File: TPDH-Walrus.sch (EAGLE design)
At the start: 34 parts, among them Q2 DMG3404, U1 MS5803-14BA, U2 SN65HVD33RHL

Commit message: PTH ISP, more routing
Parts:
- ISP1: value AVRISP -> AVRISP-6; device bschulz:AVRISP -> bschulz:AVRISP-6
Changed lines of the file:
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@@
 <part name="GND2" library="SparkFun-PowerSymbols" library_urn="urn:adsk.eagle:library:530" deviceset="GND" device=""/>
 <part name="H2" library="bschulz" deviceset="MOUNTING_HOLE" device="2_NP"/>
-<part name="ISP1" library="bschulz" deviceset="AVRISP" device=""/>
+<part name="ISP1" library="bschulz" deviceset="AVRISP" device="-6" value="AVRISP-6"/>
 <part name="PAD1" library="wirepad" library_urn="urn:adsk.eagle:library:412" deviceset="1,6/0,8" device="" package3d_urn="urn:adsk.eagle:package:30830/1"/>
 <part name="PAD2" library="wirepad" library_urn="urn:adsk.eagle:library:412" deviceset="1,6/0,8" device="" package3d_urn="urn:adsk.eagle:package:30830/1"/>

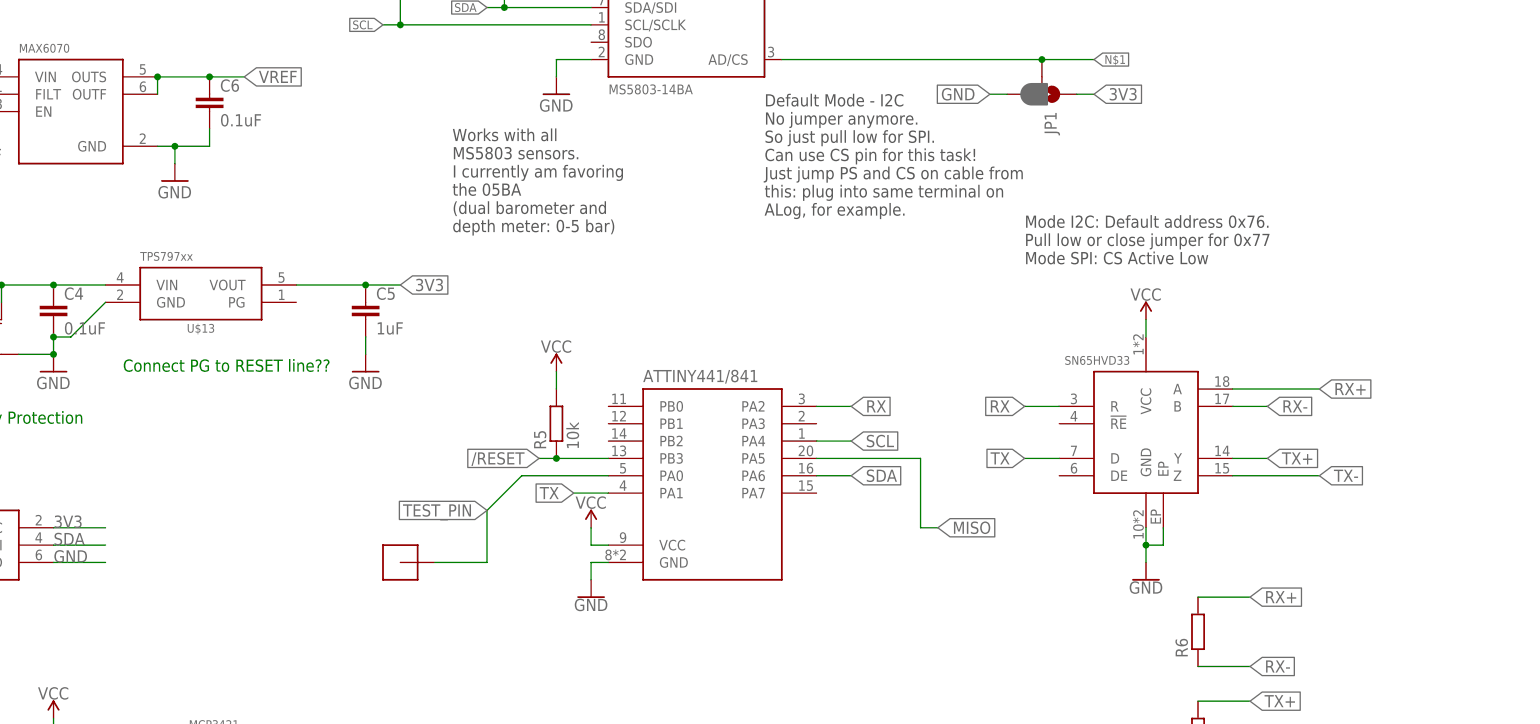
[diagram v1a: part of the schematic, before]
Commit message: multiple schematic and layout updates * status indicator * LDO reset * move thermistor by power supply and voltage reference * rip up traces and reorganize
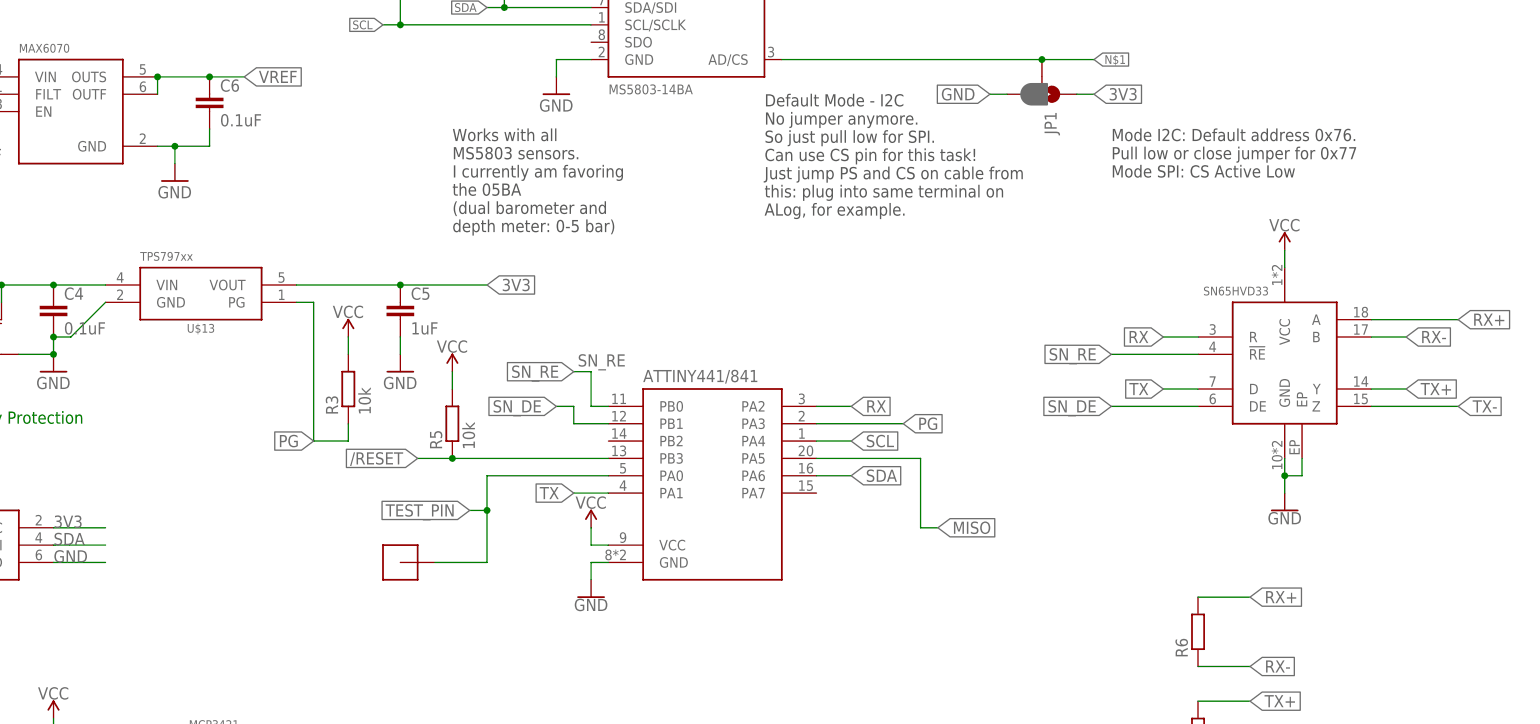
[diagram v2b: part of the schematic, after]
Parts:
- added R3: 10k, bschulz_passives:R-EU_10KR0402
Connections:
- new net PG: R3.1, U$13.PG, U$4.PA3
- new net SN_DE: U$4.PB1, U2.DE
- new net SN_RE: U$4.PB0, U2.!RE
- new net VCC: R3.2
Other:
- note removed: "Connect PG to RESET line??"
- moved on the sheet: C5, R5

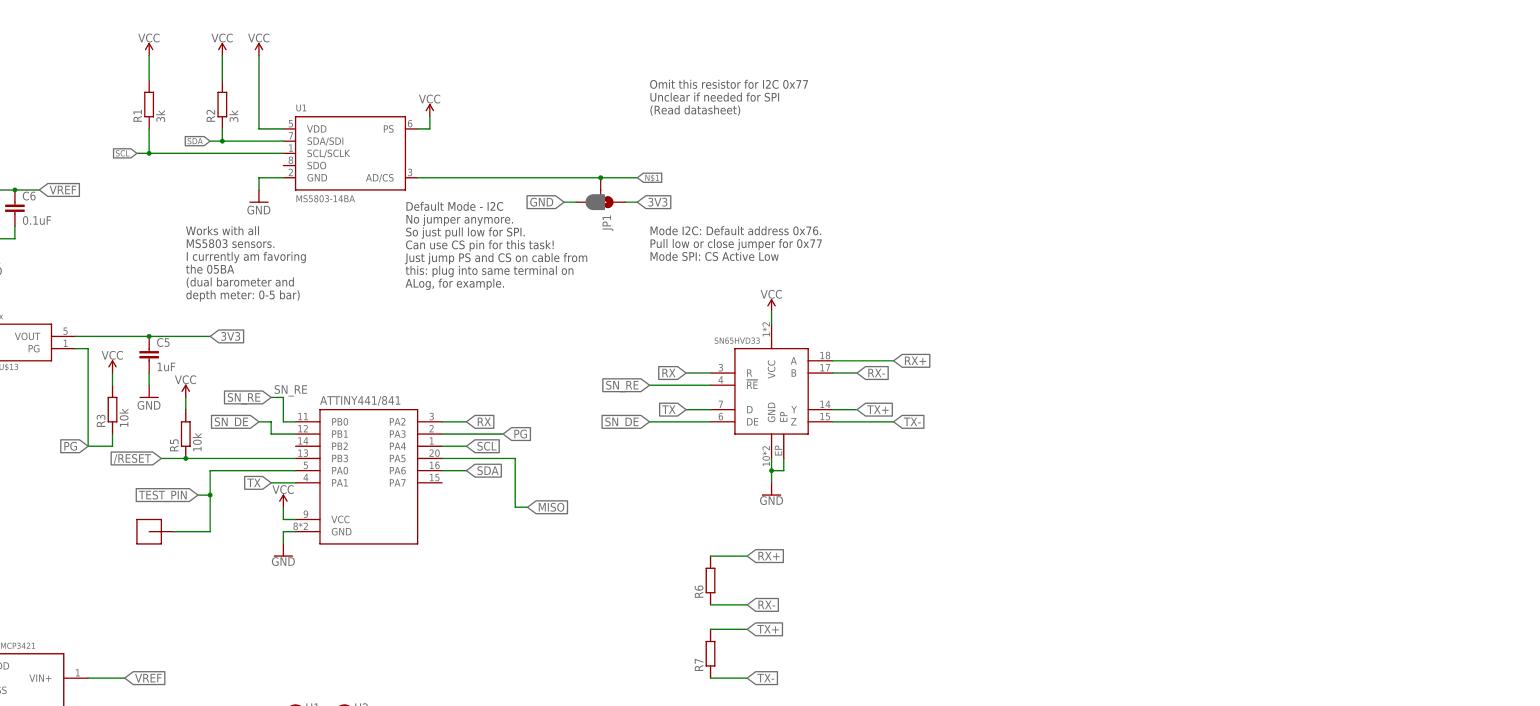
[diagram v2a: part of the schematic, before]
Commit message: ATTiny1634 on schematic
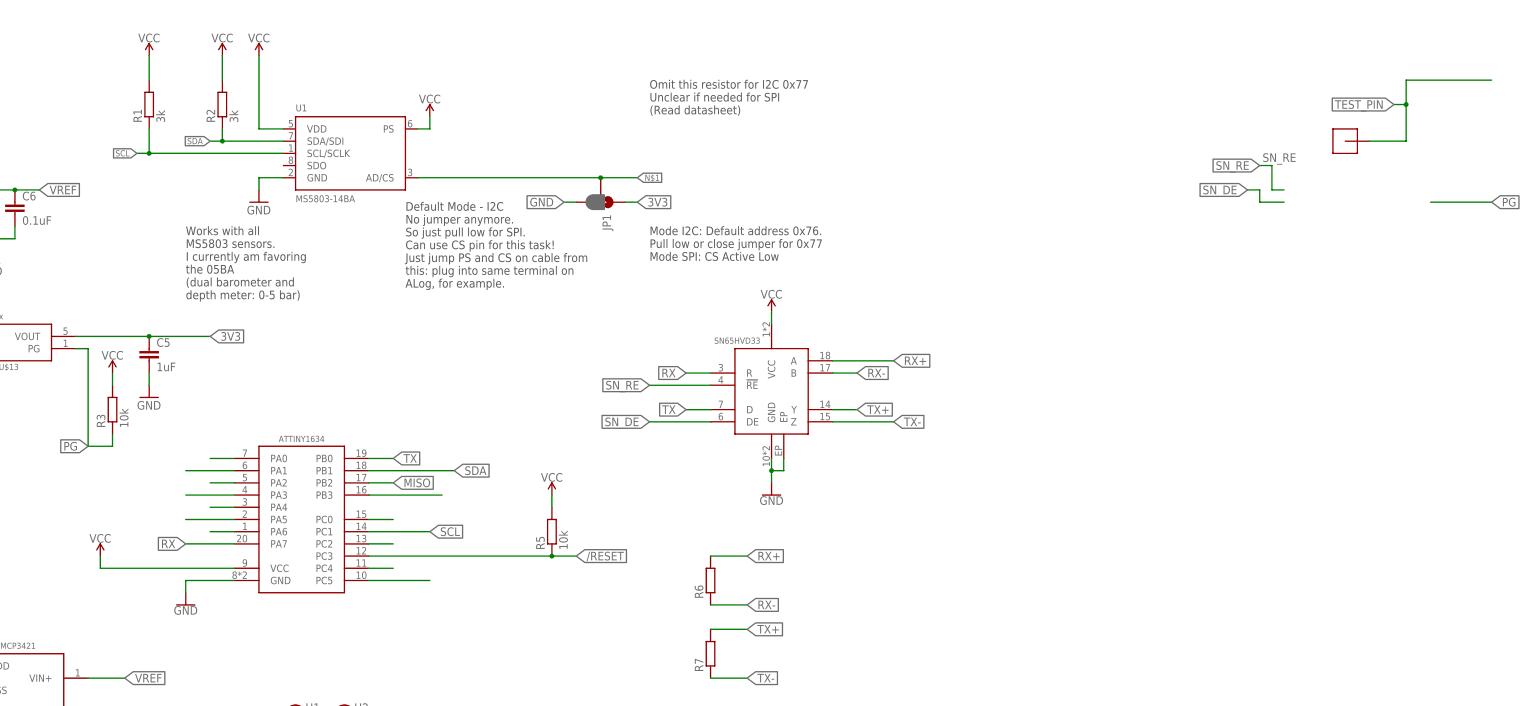
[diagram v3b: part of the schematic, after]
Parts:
- removed U$4: ATTINY441/841VQFN, bschulz:ATTINY441/841VQFN
- added U3: (no value), bschulz:ATTINY1634QFN
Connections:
- new net N$10: U3.PC4
- new net N$12: U3.PC5
- new net N$13: U3.PA4
- new net N$14: U3.PA5
- new net N$15: U3.PA6
- new net N$2: U3.PA0
- new net N$3: U3.PA1
- new net N$5: U3.PB3
- new net N$6: U3.PC0
- new net N$7: U3.PA2
- new net N$8: U3.PC2
- new net N$9: U3.PA3
- net /RESET: now also U3.PC3; no longer U$4.PB3
- net 3V3: now also U3.VCC; no longer U$4.VCC
- net GND: now also U3.GND; no longer U$4.GND
- net MISO: now also U3.PB2; no longer U$4.PA5
- net PG: no longer U$4.PA3
- net RX: now also U3.PA7; no longer U$4.PA2
- net SCL: now also U3.PC1; no longer U$4.PA4
- net SDA: now also U3.PB1; no longer U$4.PA6
- net SN_DE: no longer U$4.PB1
- net SN_RE: no longer U$4.PB0
- net TEST_PIN: no longer U$4.PA0
- net TX: now also U3.PB0; no longer U$4.PA1
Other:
- moved on the sheet: R5

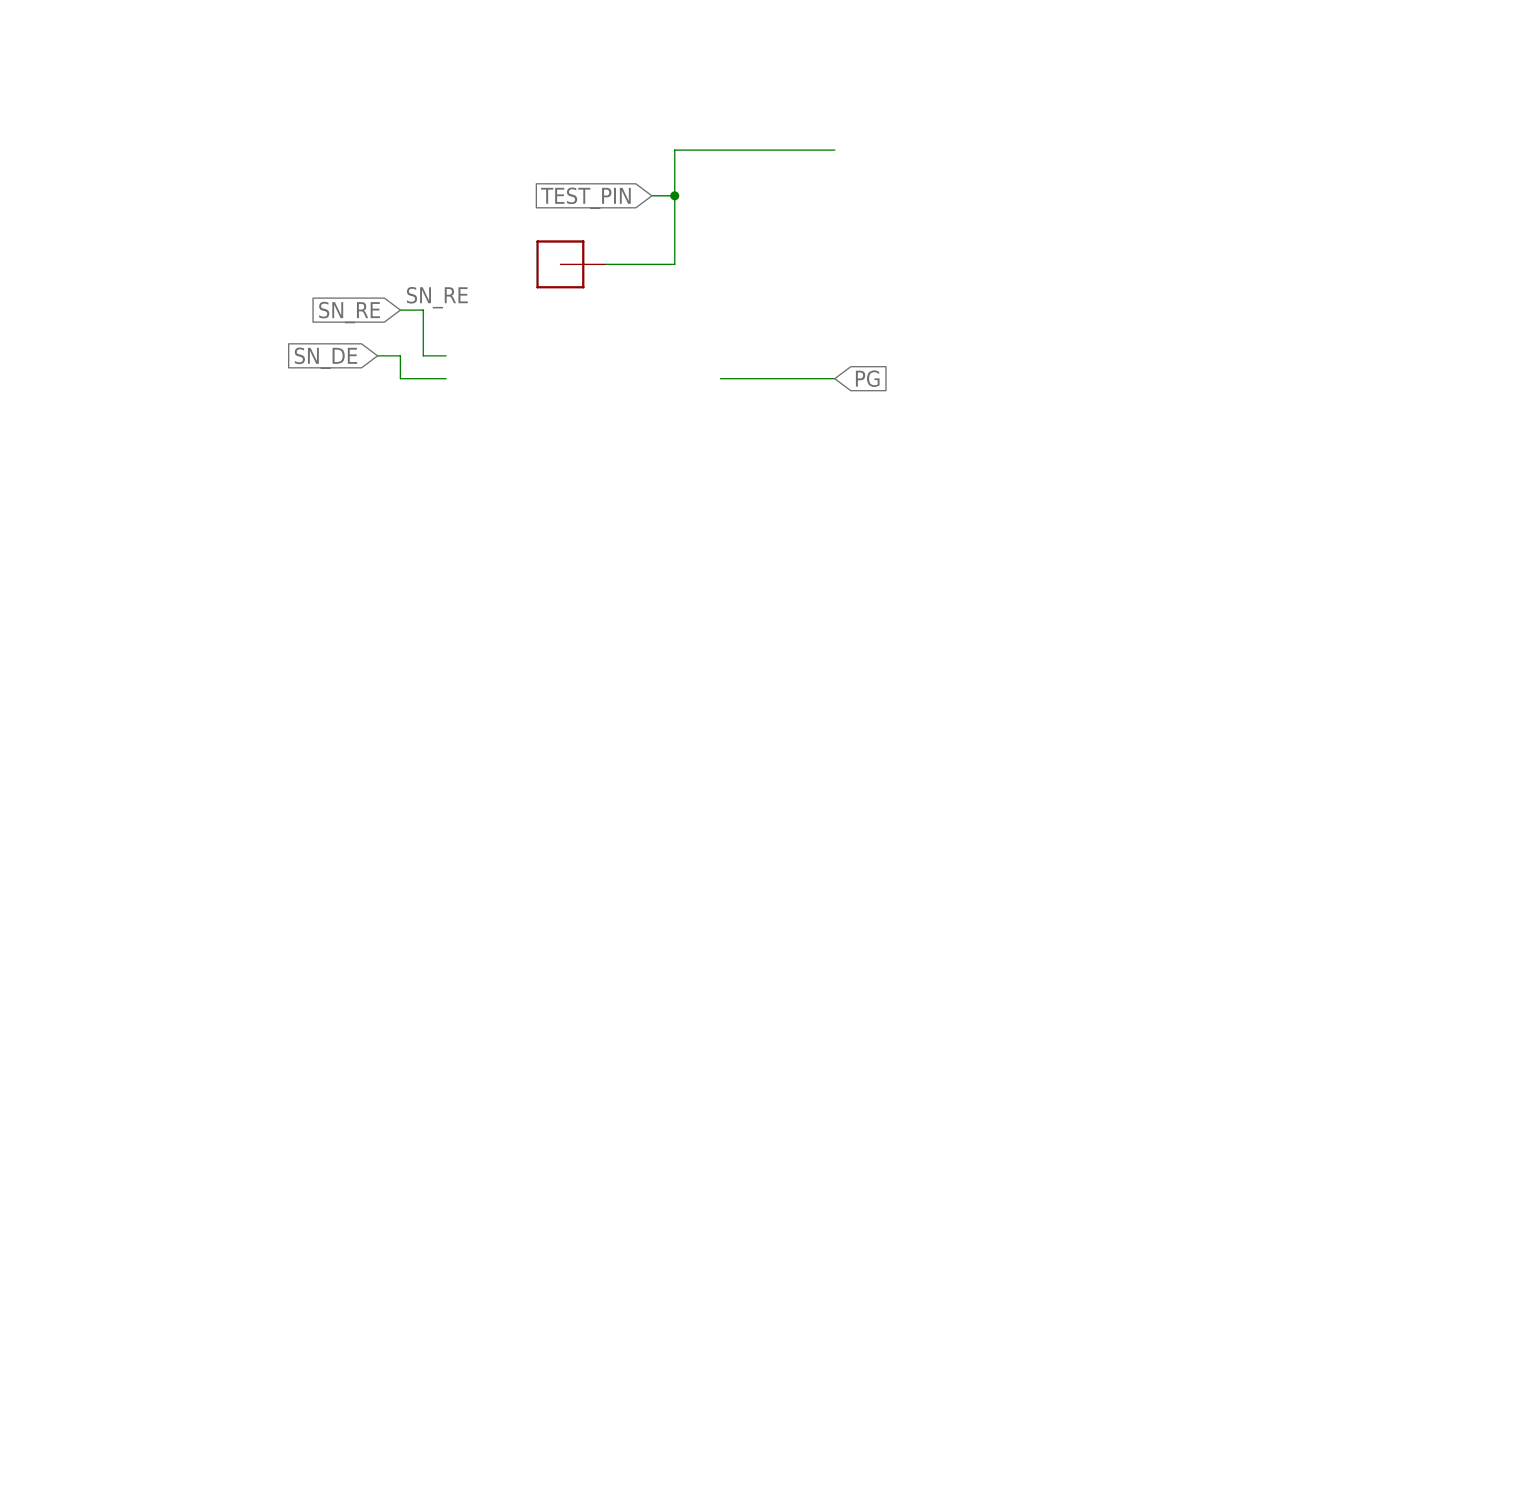
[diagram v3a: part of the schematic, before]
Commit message: Level shifter on schematic
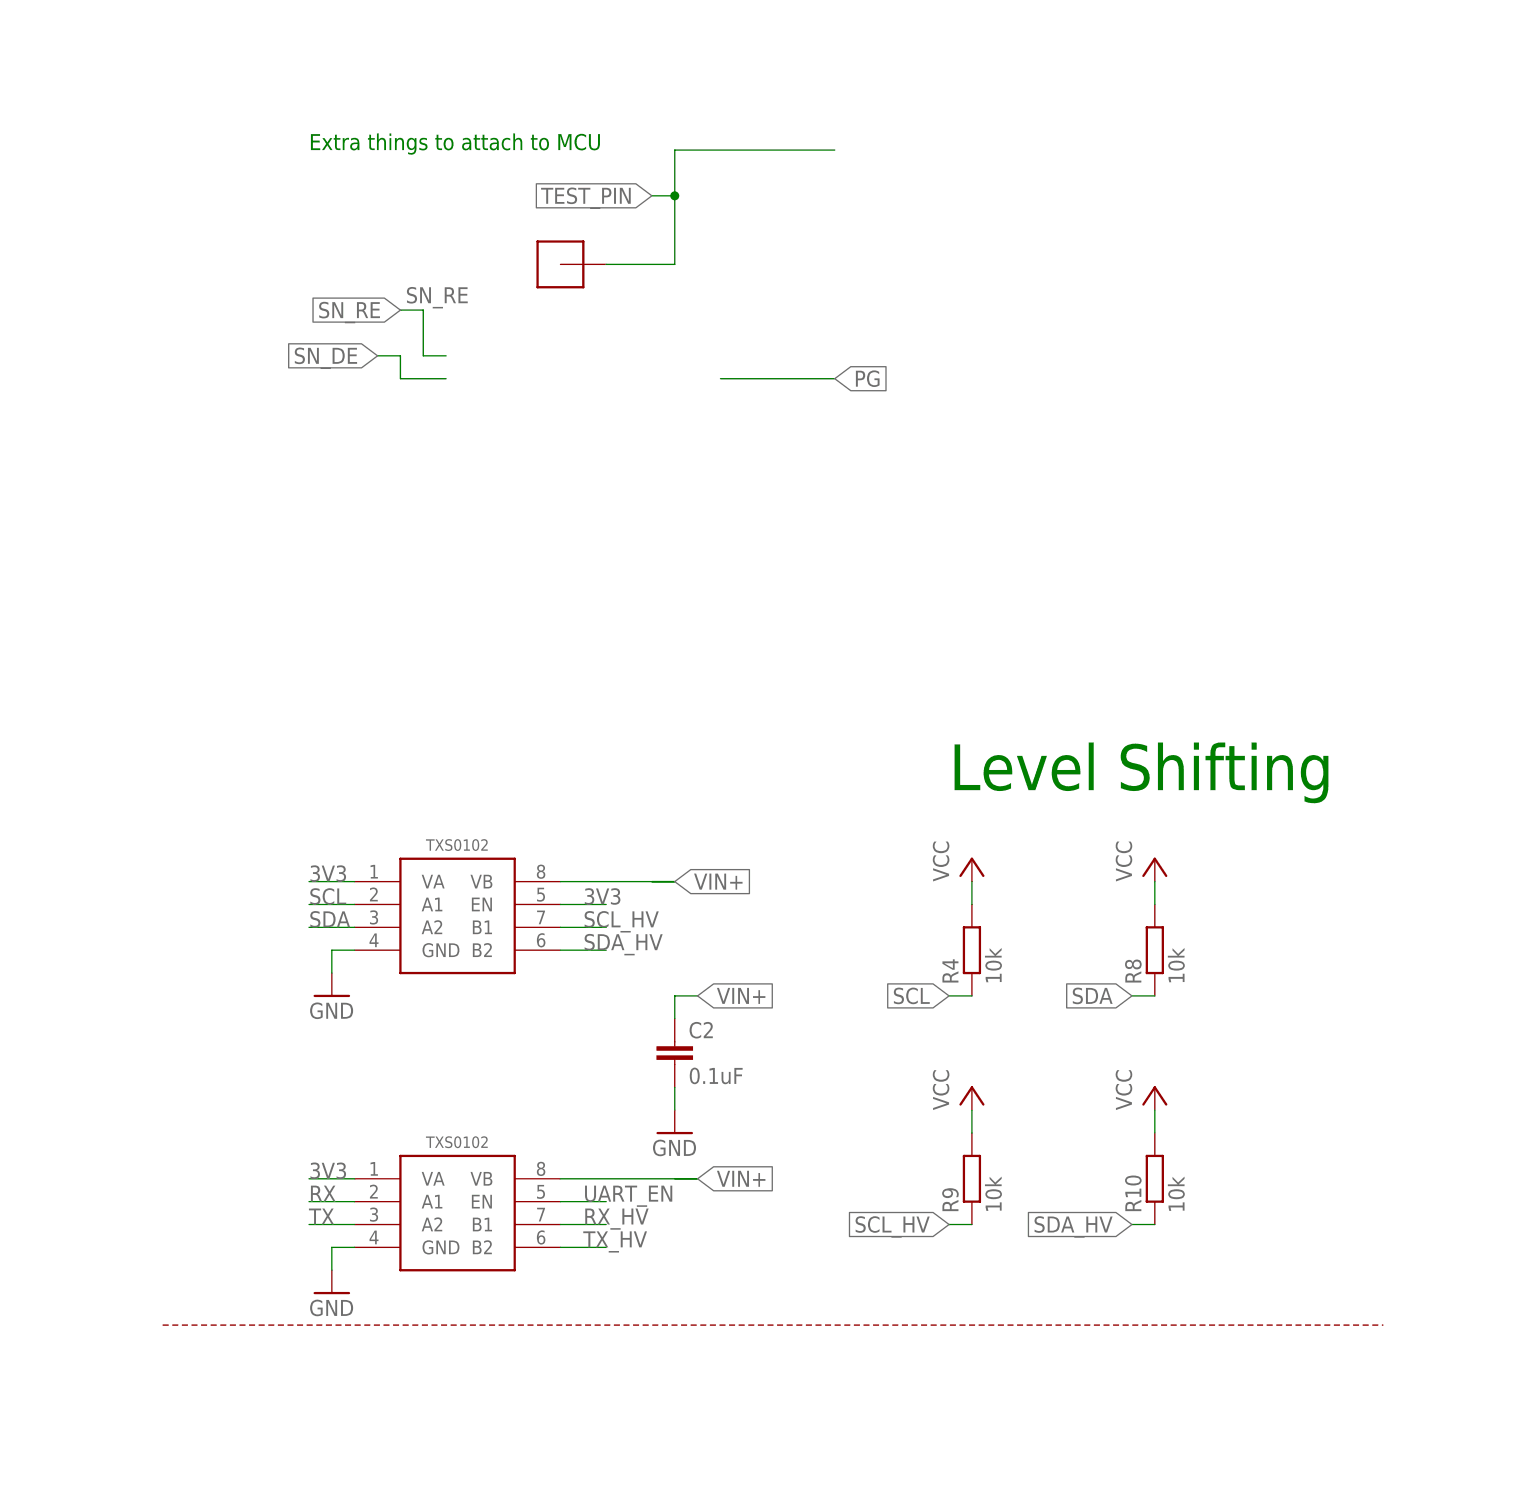
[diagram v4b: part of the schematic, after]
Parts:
- added C2: 0.1uF, bschulz_passives:C-EU0.1UFC0402
- added R10, R4, R8, R9: 10k, bschulz_passives:R-EU_10KR0402
- added U$3, U$6: TXS0102DQM, bschulz:TXS0102DQM
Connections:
- removed net VCC: R3.2
- new net RX_HV: U$6.B1
- new net SCL_HV: R9.1, U$3.B1
- new net SDA_HV: R10.1, U$3.B2
- new net TX_HV: U$6.B2
- new net UART_EN: U$6.EN
- net 3V3: now also R3.2, R4.2, R8.2, U$3.EN, U$3.VA, U$6.VA
- net GND: now also C2.2, U$3.GND, U$6.GND
- net RX: now also U$6.A1
- net SCL: now also R4.1, U$3.A1
- net SDA: now also R8.1, U$3.A2
- net TX: now also U$6.A2
- net VIN+: now also C2.1, R10.2, R9.2, U$3.VB, U$6.VB
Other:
- note added: "Extra things to attach to MCU"
- note added: "Level Shifting"

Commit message: Connected level shifter, added passives
Added schematic connections for level shifter, also added decoupling capacitors and relabeled IC values
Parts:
- removed R10, R9: 10k, bschulz_passives:R-EU_10KR0402
- removed U$6: TXS0102DQM, bschulz:TXS0102DQM
- added C10, C3, C8, C9: 0.1uF, bschulz_passives:C-EU0.1UFC0402
- R1, R2: value 3k -> 4.7k
- renumbered U$13 to U5, U$14 to U6, U$2 to U4, U$3 to U7
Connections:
- removed net RX_HV: U$6.B1
- removed net TX_HV: U$6.B2
- removed net UART_EN: U$6.EN
- new net REF_EN: U6.EN
- net 3V3: now also C10.1, C3.1, C8.1, C9.1; no longer R4.2, R8.2, U$6.VA, U6.EN
- net GND: now also C10.2, C3.2, C8.2, C9.2; no longer U$6.GND
- net RX: no longer U$6.A1
- net SCL: no longer PAD9.P, R4.1
- net SCL_HV: now also PAD9.P, R4.1; no longer R9.1
- net SDA: no longer PAD8.P, R8.1
- net SDA_HV: now also PAD8.P, R8.1; no longer R10.1
- net TX: no longer U$6.A2
- net VIN+: now also R4.2, R8.2; no longer R10.2, R9.2, U$6.VB
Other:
- note removed: "Omit this resistor for I2C 0x77 Unclear if needed for SPI (Read datasheet)"
- moved on the sheet: C2, C7

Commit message: Routed
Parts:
- added H3: (no value), bschulz:MOUNTING_HOLE2_NP
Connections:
- removed net N$12: U3.PC5
- removed net N$13: U3.PA4
- removed net N$3: U3.PA1
- removed net N$5: U3.PB3
- removed net N$6: U3.PC0
- net PG: now also U3.PA1
- net REF_EN: now also U3.PA4
- net SN_DE: now also U3.PC0
- net SN_RE: now also U3.PB3
- net TEST_PIN: now also U3.PC5
